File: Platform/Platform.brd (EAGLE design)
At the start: 67 x 67.2 mm, 34 parts, among them U1 FT232RLSSOP, X1 USBSMD, Y1 RESONATORSMD

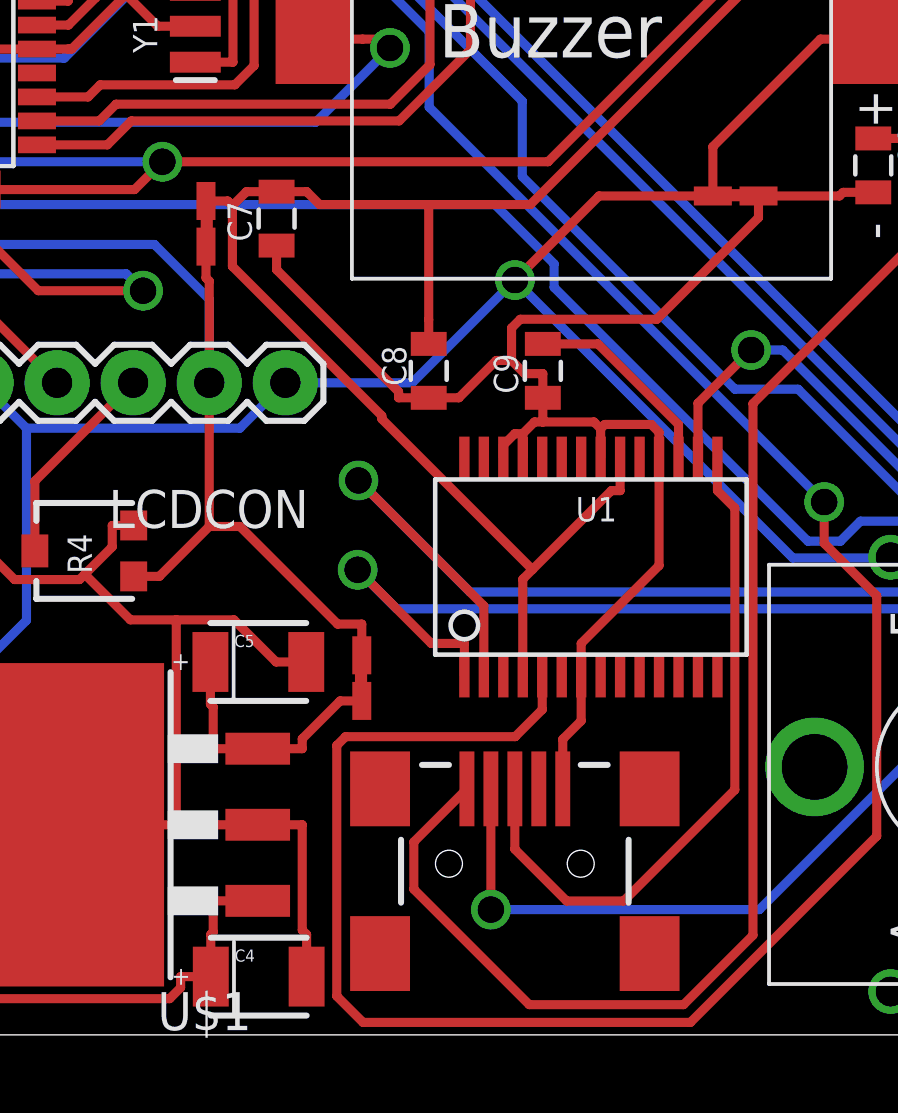
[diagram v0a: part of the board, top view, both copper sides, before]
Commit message: Added DIGIKEY# attribute to parts and generated BOM
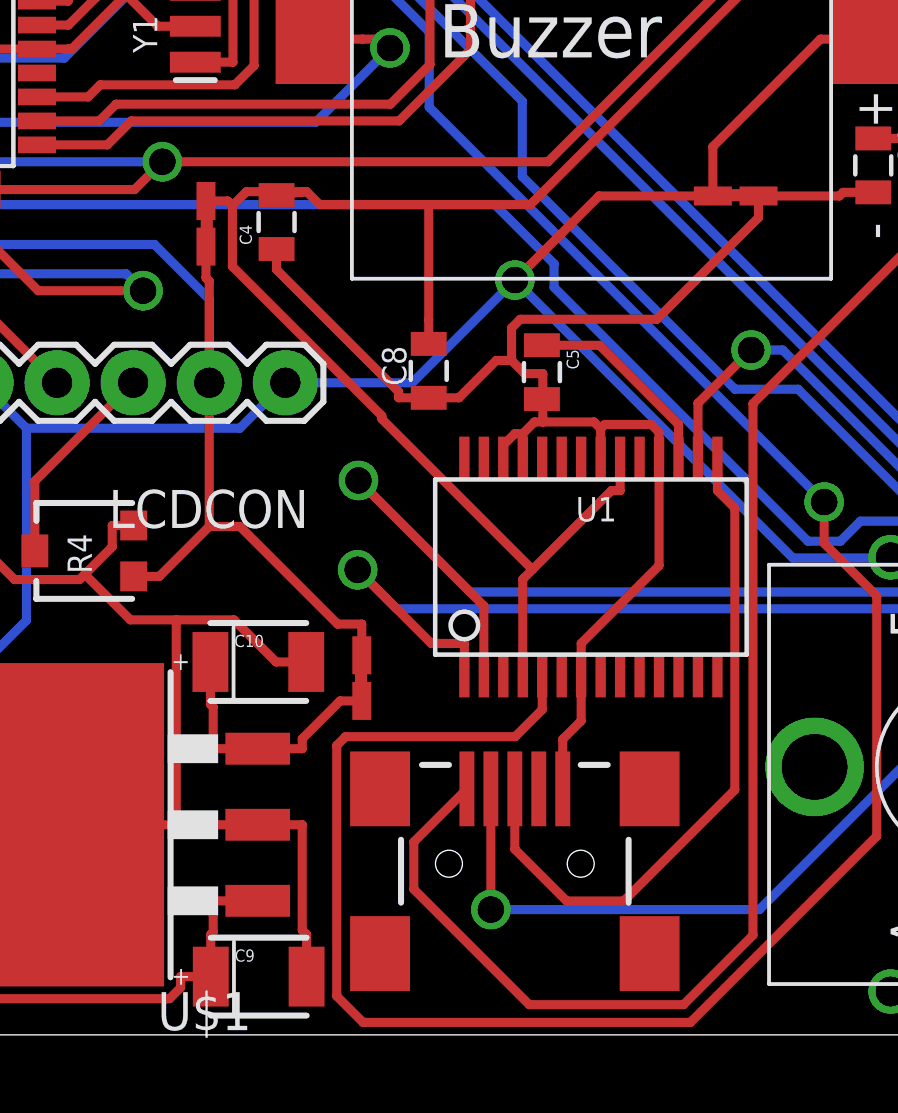
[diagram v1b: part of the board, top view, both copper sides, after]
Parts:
- removed C7: 0.1uf, SparkFun:0805
- added C10: 22UF 16V 478-1682-1-ND, Dustin:1210POL
- C4, C5: value 22UF 16V 478-1682-1-ND -> 0.1uF; device Dustin:1210POL -> SparkFun:0805
- C9: value 0.1uf -> 22UF 16V 478-1682-1-ND; device SparkFun:0805 -> Dustin:1210POL
- moved C4 25.2 mm to (35.4, 27.2), turned to 90 degrees
- moved C9 22.3 mm to (34.8, 2.01), turned to 0 degrees
- moved C5 13.5 mm to (44.3, 22.2), turned to 270 degrees
- renumbered U$3 to FB
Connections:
- net 3V3OUT: now also C5.1; no longer C9.2
- net FTDI-GND: now also C4.1, C5.2; no longer C7.1, C9.1
- net FTDI-VCC: now also C4.2; no longer C7.2
- net GND: now also C10.2, C9.2; no longer C4.2, C5.2
- net LDO_OUT: now also C10.1; no longer C5.1
- net RAW_IN: now also C9.1; no longer C4.1
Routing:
- net FTDI-VCC: track 65.8 -> 66.8 mm

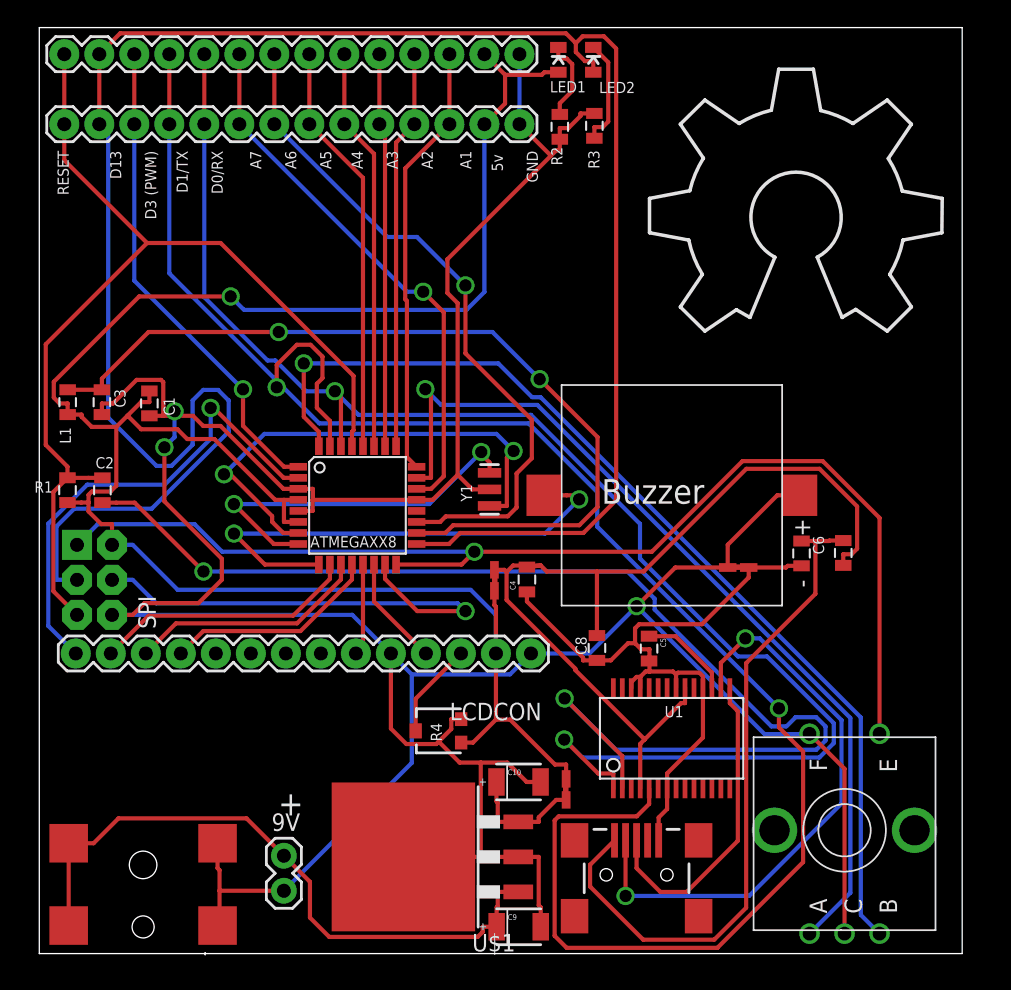
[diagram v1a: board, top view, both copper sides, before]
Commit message: added dimensions, reference drawing for lcd
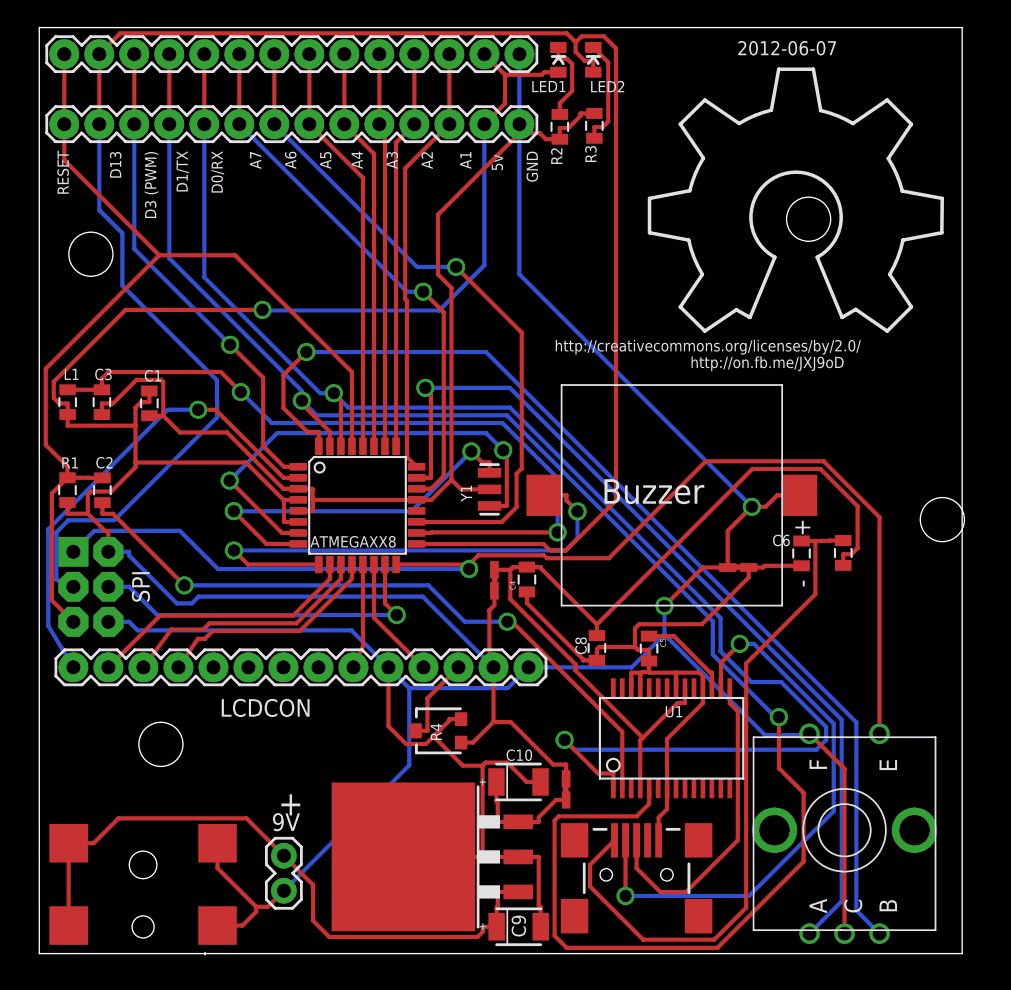
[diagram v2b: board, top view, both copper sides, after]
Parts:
- added U$3: LCM-S01602DTR, Dustin:LCD16X2
- moved LCDCON 1.02 mm to (35.6, 20.8)
- moved SPI 0.57 mm to (3.81, 26.7)
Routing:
- net DTR: track 90.3 -> 49.2 mm
- net D13/SCK: track 154.8 -> 140.7 mm
- net GND: track 266.1 -> 276.3 mm, vias 3 -> 2
- net TX: track 137.7 -> 127.9 mm
- net AVCC: track 62.8 -> 53.9 mm
- net D11/MOSI: track 34.4 -> 25.8 mm
- net RX: track 109.4 -> 106.4 mm
- net D2: track 73.8 -> 76.1 mm
- net XTAL1: track 35.6 -> 33.7 mm
- net FTDI-VCC: track 66.8 -> 65.0 mm
- net VCC: track 151.5 -> 149.8 mm
- net D-: track 42.3 -> 41.0 mm
- net D5: track 35.9 -> 37.0 mm
- net D4: track 35.3 -> 34.3 mm
- net FTDI-GND: track 50.7 -> 51.7 mm
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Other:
- board text added: "2012-06-07"
- board text removed: "2012-05-12"

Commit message: Prototype 5 changes
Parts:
- moved R3 4.55 mm to (44.9, 60.1)
- moved LED1 4.55 mm to (42.3, 64.9)
- moved LED2 4.55 mm to (44.8, 64.9)
- moved R2 4.55 mm to (42.4, 60.0)
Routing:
- net AVCC: track 53.9 -> 64.9 mm
- net D4: track 34.3 -> 26.5 mm, vias 1 -> 0
- net GND: track 276.3 -> 280.3 mm
- net VCC: track 149.8 -> 153.3 mm, vias 1 -> 2
- net D13/SCK: track 140.7 -> 138.5 mm
- net D2: track 76.1 -> 74.9 mm
- net XTAL1: track 33.7 -> 35.0 mm
- net D5: track 37.0 -> 35.8 mm
- net RESET: track 74.6 -> 75.2 mm
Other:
- board text added: "2012-06-14"
- board text removed: "2012-06-07"
